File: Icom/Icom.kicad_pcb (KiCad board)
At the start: 2 copper layers, 38.1 x 31.8 mm, 8 parts, among them J1 OHIS RJ45, J2 Icom RJ45 Mic, J4 Headphone In, J5 Speaker Input Config

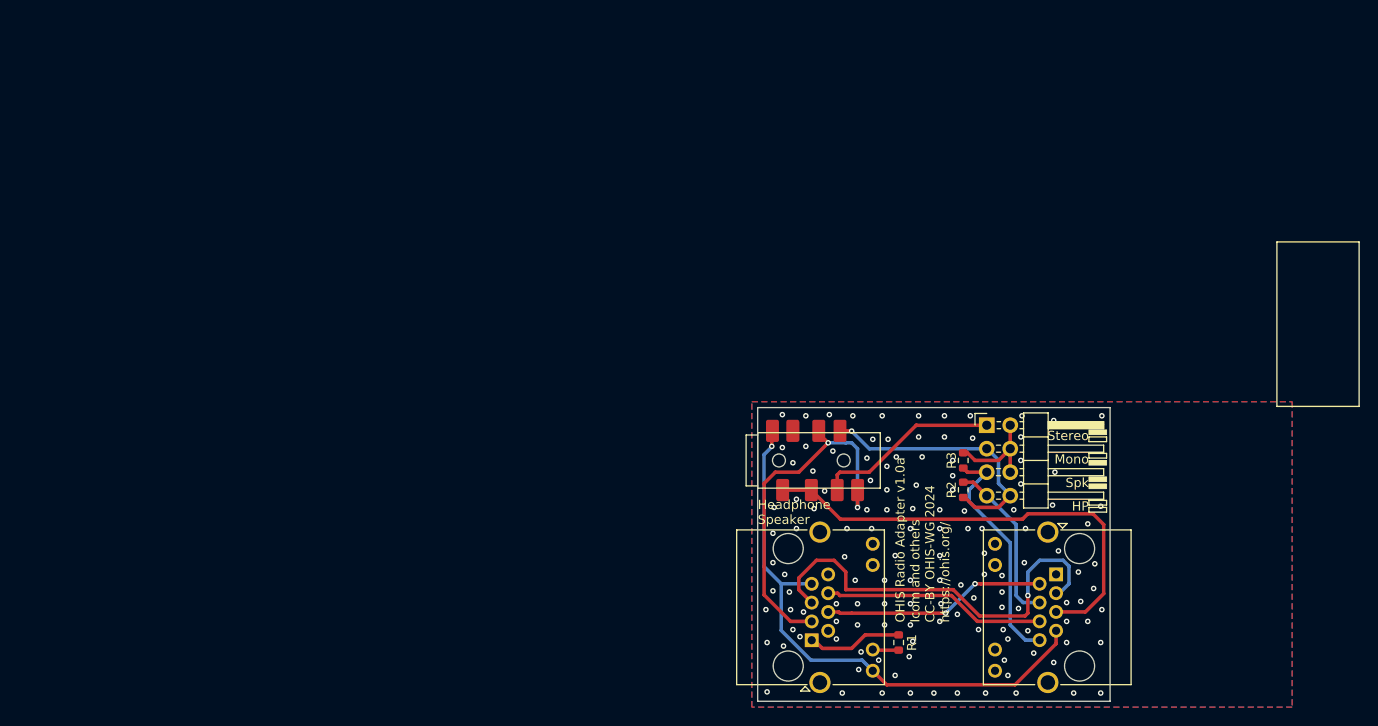
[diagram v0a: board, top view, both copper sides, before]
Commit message: For #1. Looks much more like the User Adapter.
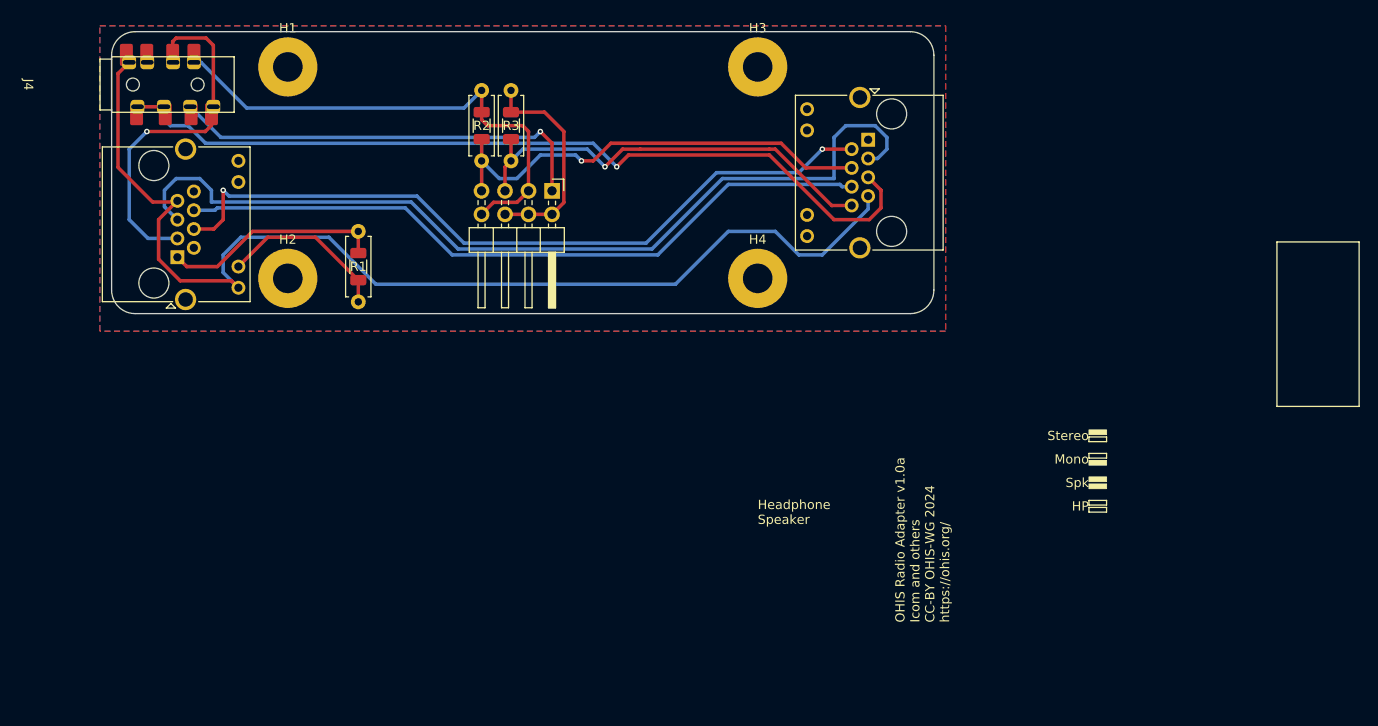
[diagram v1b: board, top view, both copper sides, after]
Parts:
- added H1: MountingHole_Pad, MountingHole:MountingHole_3.2mm_M3_Pad, F.Cu at (63.5, 33.0)
- added H2: MountingHole_Pad, MountingHole:MountingHole_3.2mm_M3_Pad, F.Cu at (63.5, 55.9)
- added H3: MountingHole_Pad, MountingHole:MountingHole_3.2mm_M3_Pad, F.Cu at (114.3, 33.0)
- added H4: MountingHole_Pad, MountingHole:MountingHole_3.2mm_M3_Pad, F.Cu at (114.3, 55.9)
- added R4: 100R, Resistor_THT:R_Axial_DIN0207_L6.3mm_D2.5mm_P7.62mm_Horizontal, F.Cu at (84.5, 43.2)
- added R5: 100R, Resistor_THT:R_Axial_DIN0207_L6.3mm_D2.5mm_P7.62mm_Horizontal, F.Cu at (87.6, 35.6)
- added R6: 2.2k, Resistor_THT:R_Axial_DIN0207_L6.3mm_D2.5mm_P7.62mm_Horizontal, F.Cu at (71.1, 50.8)
- J4: footprint Libraries:Conn_3.5mm-PJ-393_C2837065_C668609_C128990 -> Libraries:Conn_3.5mm-PJ-393_SMT-C668609_TH-C145811
- R1, R2, R3: footprint Resistor_SMD:R_0603_1608Metric -> Resistor_SMD:R_1206_3216Metric
- moved J4 80.8 mm to (44.5, 34.9)
- moved J2 80.1 mm to (51.6, 53.6)
- moved R1 71.2 mm to (71.1, 54.6)
- moved R2 65.3 mm to (84.5, 39.4), turned to 90 degrees
- moved R3 60.8 mm to (87.6, 39.4)
- moved J5 53.4 mm to (92.1, 46.4), turned to -90 degrees
- moved J1 51.2 mm to (126.2, 40.9)
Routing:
- net Power Gnd: track 61.5 -> 121.6 mm, vias 1 -> 0
- net ~{PTT}: track 24.2 -> 81.3 mm
- net Mic Gnd: track 45.9 -> 98.7 mm, vias 1 -> 0
- net Mic+: track 24.1 -> 76.6 mm
- net HP Gnd: track 50.2 -> 91.7 mm, vias 0 -> 1
- net HP Left: track 18.1 -> 49.6 mm, vias 0 -> 1
- net Net-(J5-Pin_3): track 28.9 -> 56.1 mm, vias 1 -> 0
- net Net-(J5-Pin_1): track 20.1 -> 46.4 mm, vias 0 -> 1
- net HP Right: track 25.7 -> 47.3 mm, vias 0 -> 1
- net Net-(J2-Pad10): track 2.83 -> 18.5 mm
- net +8v 10mA: track 10.4 -> 23.9 mm
- net Net-(J5-Pin_2): track 11.1 -> 23.5 mm
- net AF Out: track 40.5 -> 39.5 mm, vias 2 -> 1
- net Shield: vias 131 -> 0
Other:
- board size 38.1 x 31.8 mm -> 88.9 x 30.5 mm

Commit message: Kenwood laid out more similarly to the User Adapter. #1
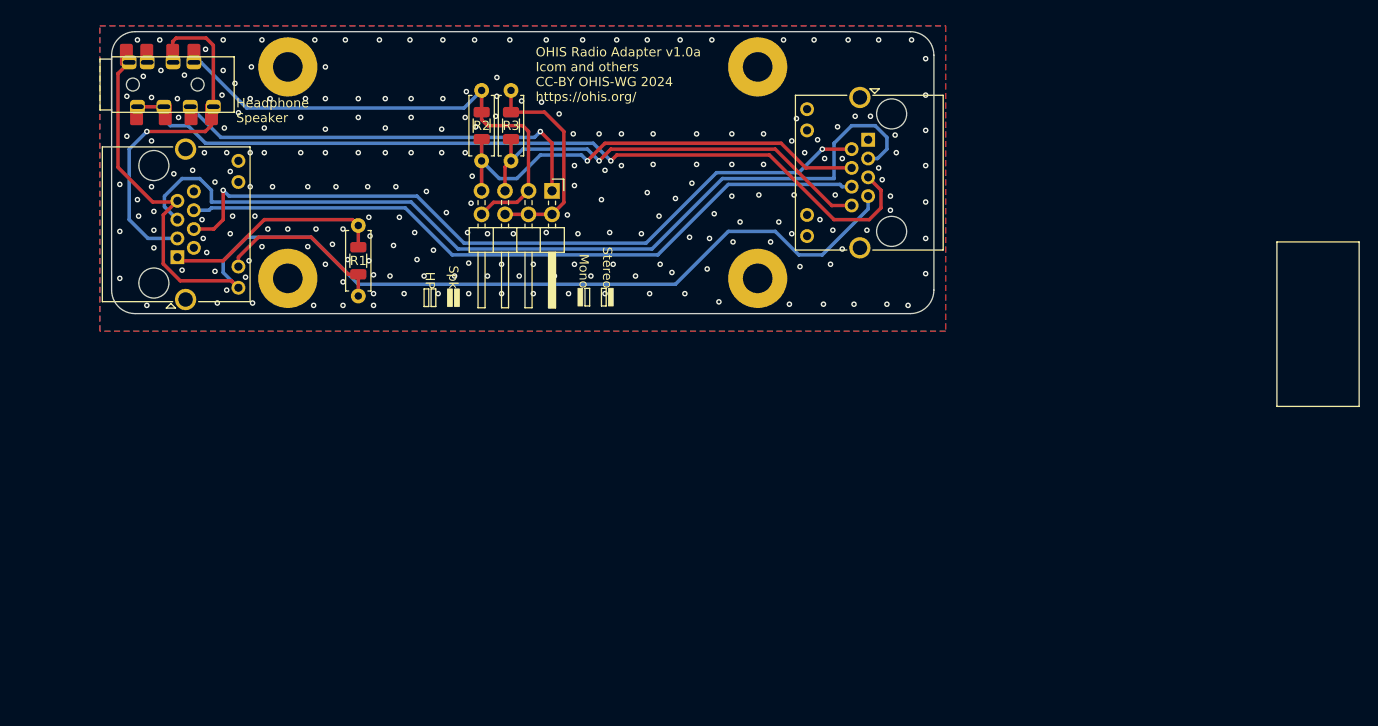
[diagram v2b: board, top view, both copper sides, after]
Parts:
- moved G1 50.9 mm to (131.1, 44.5)
- moved R1 0.63 mm to (71.1, 54.0)
- moved R6 0.63 mm to (71.1, 50.2)
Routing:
- net Power Gnd: track 121.6 -> 120.8 mm
- net Mic Gnd: track 98.7 -> 97.9 mm
- net HP Gnd: track 91.7 -> 91.2 mm
- net HP Right: track 47.3 -> 46.8 mm
- net Shield: vias 0 -> 233
